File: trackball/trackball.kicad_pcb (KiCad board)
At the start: 2 copper layers, 15 x 13.4 mm, 13 parts, among them P8 CONN_7, U1 BU52012HFV-TR, U2 BU52012HFV-TR, U3 BU52012HFV-TR, U4 BU52012HFV-TR

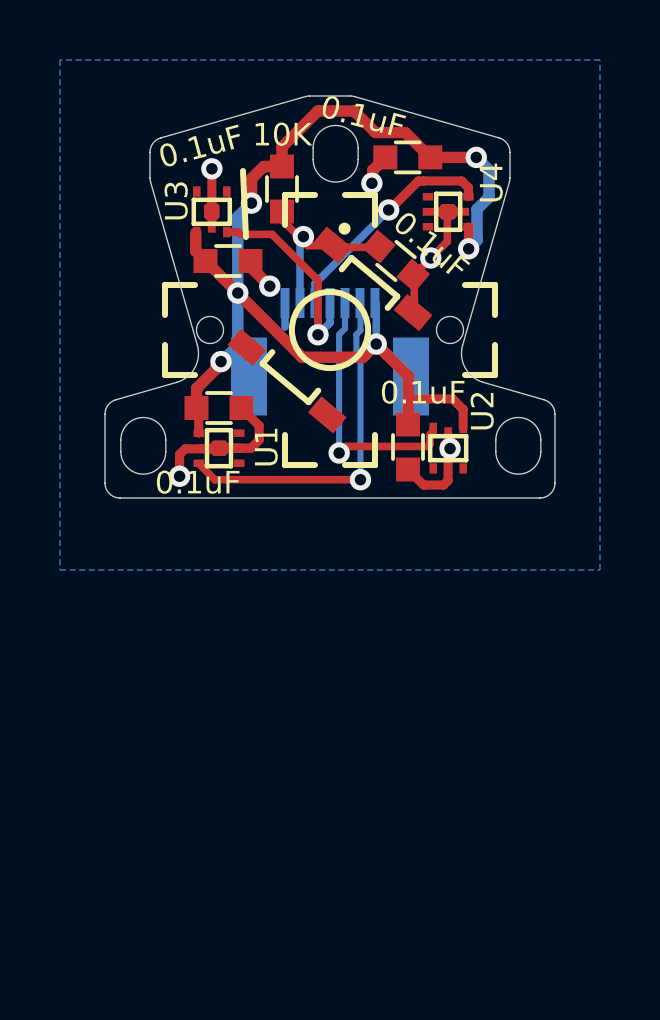
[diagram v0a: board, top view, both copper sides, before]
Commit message: Leave more space at the bottom of the board.
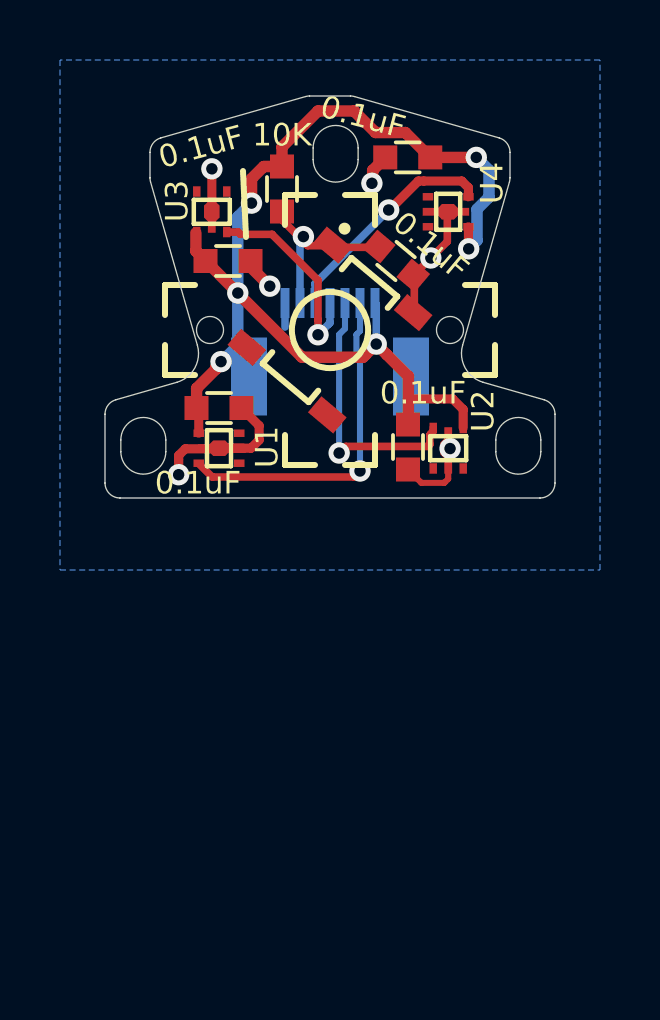
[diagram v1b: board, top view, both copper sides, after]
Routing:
- net GND: track 17.1 -> 16.5 mm
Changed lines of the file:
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@@
     (thickness 1.6)
     (drawings 42)
-    (tracks 140)
+    (tracks 141)
     (zones 0)
     (modules 13)
@@
     (pad_to_mask_clearance 0)
     (aux_axis_origin 0 0)
-    (visible_elements 7FFFEF7F)
+    (visible_elements 7FFFFF7F)
     (pcbplotparams
       (layerselection 0x00030_ffffffff)
@@
   (via (at 196.0626 144.627598) (size 0.7112) (drill 0.381) (layers F.Cu B.Cu) (net 1))
   (segment (start 196.0626 146.0754) (end 196.0626 144.627598) (width 0.3048) (layer F.Cu) (net 1))
-  (segment (start 203.1186 155.1686) (end 202.6 154.65) (width 0.3048) (layer F.Cu) (net 1))
-  (segment (start 203.7842 155.1686) (end 203.1186 155.1686) (width 0.3048) (layer F.Cu) (net 1))
-  (segment (start 203.9366 153.9494) (end 203.9366 155.0162) (width 0.3048) (layer F.Cu) (net 1))
-  (segment (start 203.9366 155.0162) (end 203.7842 155.1686) (width 0.3048) (layer F.Cu) (net 1))
   (via (at 197.993 148.5392) (size 0.7112) (drill 0.381) (layers F.Cu B.Cu) (net 1))
   (segment (start 197.35 147.8962) (end 197.993 148.5392) (width 0.381) (layer F.Cu) (net 1))
@@
   (segment (start 201.8404 144.26) (end 201.422 144.6784) (width 0.381) (layer F.Cu) (net 1))
   (via (at 204.002044 153.951866) (size 0.7112) (drill 0.381) (layers F.Cu B.Cu) (net 1))
-  (via (at 194.986061 154.876501) (size 0.7112) (drill 0.381) (layers F.Cu B.Cu) (net 1))
+  (segment (start 198.5 149.1) (end 198.5 149.9) (width 0.254) (layer B.Cu) (net 1))
+  (via (at 194.95467 154.823689) (size 0.7112) (drill 0.381) (layers F.Cu B.Cu) (net 1))
   (segment (start 196.3 153.94) (end 196.280601 153.959399) (width 0.3048) (layer F.Cu) (net 1))
   (segment (start 196.280601 153.959399) (end 195.178044 153.959399) (width 0.3048) (layer F.Cu) (net 1))
-  (segment (start 195.178044 153.959399) (end 194.986061 154.151382) (width 0.3048) (layer F.Cu) (net 1))
-  (segment (start 194.986061 154.373607) (end 194.986061 154.876501) (width 0.3048) (layer F.Cu) (net 1))
-  (segment (start 194.986061 154.151382) (end 194.986061 154.373607) (width 0.3048) (layer F.Cu) (net 1))
-  (segment (start 198.5 149.1) (end 198.5 149.9) (width 0.254) (layer B.Cu) (net 1))
+  (segment (start 195.178044 153.959399) (end 194.95467 154.182773) (width 0.3048) (layer F.Cu) (net 1))
+  (segment (start 194.95467 154.320795) (end 194.95467 154.823689) (width 0.3048) (layer F.Cu) (net 1))
+  (segment (start 194.95467 154.182773) (end 194.95467 154.320795) (width 0.3048) (layer F.Cu) (net 1))
+  (segment (start 203.808841 155.094801) (end 203.94 154.963642) (width 0.2032) (layer F.Cu) (net 1))
+  (segment (start 202.6 154.65) (end 203.044801 155.094801) (width 0.2032) (layer F.Cu) (net 1))
+  (segment (start 203.044801 155.094801) (end 203.808841 155.094801) (width 0.2032) (layer F.Cu) (net 1))
+  (segment (start 203.94 154.963642) (end 203.94 154.46) (width 0.2032) (layer F.Cu) (net 1))
   (segment (start 200.390425 147.2438) (end 200.335876 147.189251) (width 0.254) (layer F.Cu) (net 2))
   (segment (start 201.66967 147.16967) (end 201.59554 147.2438) (width 0.254) (layer F.Cu) (net 2))
@@
   (segment (start 199.11316 146.886077) (end 199 146.999237) (width 0.254) (layer B.Cu) (net 2))
   (segment (start 199 146.999237) (end 199 149.1) (width 0.254) (layer B.Cu) (net 2))
-  (via (at 201.0156 154.9908) (size 0.7112) (drill 0.381) (layers F.Cu B.Cu) (net 3))
-  (segment (start 196.1642 154.9908) (end 201.0156 154.9908) (width 0.254) (layer F.Cu) (net 3))
-  (segment (start 195.6308 154.4574) (end 196.1642 154.9908) (width 0.254) (layer F.Cu) (net 3))
-  (segment (start 201.0156 150.01774) (end 201.0156 149.2156) (width 0.2032) (layer B.Cu) (net 3))
-  (segment (start 200.880733 150.152607) (end 201.0156 150.01774) (width 0.2032) (layer B.Cu) (net 3))
-  (segment (start 200.880733 150.786593) (end 200.880733 150.152607) (width 0.2032) (layer B.Cu) (net 3))
-  (segment (start 201.0156 154.9908) (end 201.0156 150.92146) (width 0.2032) (layer B.Cu) (net 3))
-  (segment (start 201.0156 150.92146) (end 200.880733 150.786593) (width 0.2032) (layer B.Cu) (net 3))
-  (segment (start 201.0156 149.2156) (end 201 149.2) (width 0.2032) (layer B.Cu) (net 3))
+  (via (at 201 154.7) (size 0.7112) (drill 0.381) (layers F.Cu B.Cu) (net 3))
+  (segment (start 200.880733 150.152607) (end 200.880733 150.786593) (width 0.2032) (layer B.Cu) (net 3))
+  (segment (start 201 150.90586) (end 201 154.197106) (width 0.2032) (layer B.Cu) (net 3))
+  (segment (start 200.880733 150.786593) (end 201 150.90586) (width 0.2032) (layer B.Cu) (net 3))
+  (segment (start 201 149.2) (end 201 150.03334) (width 0.2032) (layer B.Cu) (net 3))
+  (segment (start 201 150.03334) (end 200.880733 150.152607) (width 0.2032) (layer B.Cu) (net 3))
+  (segment (start 201 154.197106) (end 201 154.7) (width 0.2032) (layer B.Cu) (net 3))
+  (segment (start 200.8 154.9) (end 201 154.7) (width 0.254) (layer F.Cu) (net 3))
+  (segment (start 195.6308 154.4574) (end 196.0734 154.9) (width 0.254) (layer F.Cu) (net 3))
+  (segment (start 196.0734 154.9) (end 200.8 154.9) (width 0.254) (layer F.Cu) (net 3))
   (segment (start 202.6158 153.162) (end 202.6158 152.2984) (width 0.381) (layer F.Cu) (net 4))
   (segment (start 202.6158 152.2984) (end 204.089 152.2984) (width 0.3048) (layer F.Cu) (net 4))

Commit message: Remove excess resistor and capacitor.
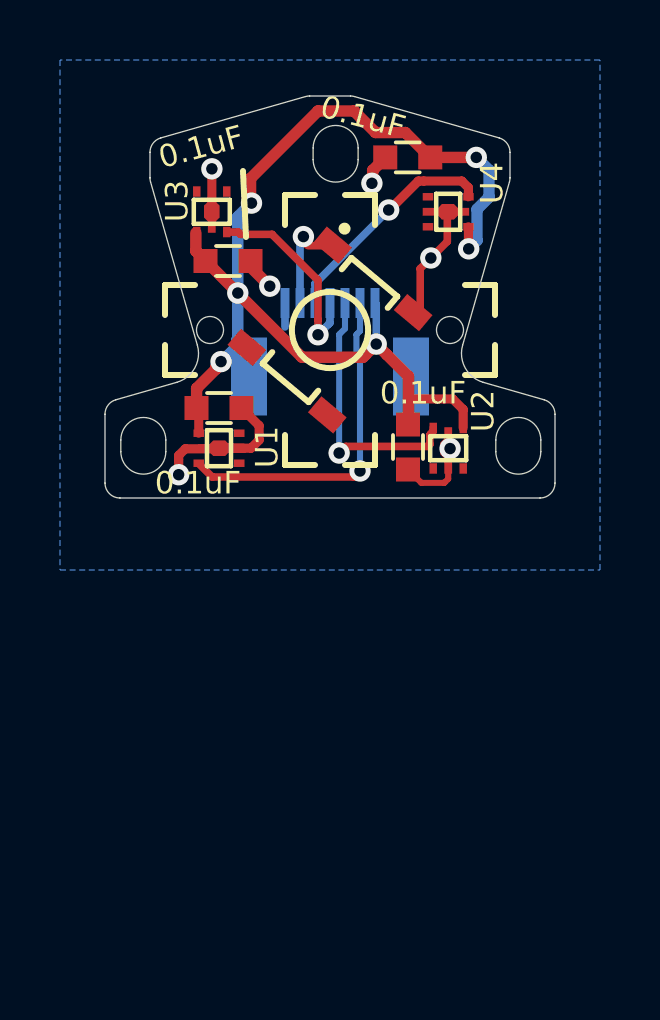
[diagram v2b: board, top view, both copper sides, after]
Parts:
- removed C5: 0.1uF, UGL:SM0603
- removed R5: 10K, UGL:SM0603
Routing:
- net /TB_BTN: track 6.82 -> 4.01 mm
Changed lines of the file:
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@@
     (thickness 1.6)
     (drawings 42)
-    (tracks 141)
+    (tracks 134)
     (zones 0)
-    (modules 13)
+    (modules 11)
     (nets 16)
   )
@@
   )
   (setup
-    (last_trace_width 0.2032)
+    (last_trace_width 0.254)
     (user_trace_width 0.2032)
     (user_trace_width 0.254)
@@
   )
   (module UGL:SM0603 (layer F.Cu)
-    (at 202.2 147.7 140)
-    (attr smd)
-    (fp_text reference C5 (at 0 0 140) (layer B.SilkS)
-      (effects (font (size 0.75 0.75) (thickness 0.15)) (justify mirror))
-    )
-    (fp_text value 0.1uF (at -0.565685 1.131371 140) (layer F.SilkS)
-      (effects (font (size 0.75 0.75) (thickness 0.15)))
-    )
-    (fp_line (start -0.4 -0.5) (end 0.4 -0.5) (layer F.SilkS) (width 0.127))
-    (fp_line (start 0.4 0.5) (end -0.4 0.5) (layer F.SilkS) (width 0.127))
-    (pad 1 smd rect (at -0.75 0 140) (size 0.8 0.8) (layers F.Cu F.Paste F.Mask)
-      (net 1 GND))
-    (pad 2 smd rect (at 0.75 0 140) (size 0.8 0.8) (layers F.Cu F.Paste F.Mask)
-      (net 2 /TB_BTN))
-    (model smd\resistors\R0603.wrl
-      (offset (xyz 0 0 0.02540000082496551))
-      (scale (xyz 0.5 0.5 0.5))
-      (rotate (xyz 0 0 0))
-    )
-  )
-  (module UGL:SM0603 (layer F.Cu)
-    (at 198.4 145.3 270)
-    (attr smd)
-    (fp_text reference R5 (at 0.1 0 270) (layer B.SilkS)
-      (effects (font (size 0.75 0.75) (thickness 0.15)) (justify mirror))
-    )
-    (fp_text value 10K (at -1.8 0) (layer F.SilkS)
-      (effects (font (size 0.75 0.75) (thickness 0.15)))
-    )
-    (fp_line (start -0.4 -0.5) (end 0.4 -0.5) (layer F.SilkS) (width 0.127))
-    (fp_line (start 0.4 0.5) (end -0.4 0.5) (layer F.SilkS) (width 0.127))
-    (pad 1 smd rect (at -0.75 0 270) (size 0.8 0.8) (layers F.Cu F.Paste F.Mask)
-      (net 4 +3V3))
-    (pad 2 smd rect (at 0.75 0 270) (size 0.8 0.8) (layers F.Cu F.Paste F.Mask)
-      (net 2 /TB_BTN))
-    (model smd\resistors\R0603.wrl
-      (offset (xyz 0 0 0.02540000082496551))
-      (scale (xyz 0.5 0.5 0.5))
-      (rotate (xyz 0 0 0))
-    )
-  )
-  (module UGL:SM0603 (layer F.Cu)
     (at 202.5904 144.2466)
     (attr smd)
@@
     (effects (font (size 0.75 0.75) (thickness 0.15)) (justify mirror))
   )
-  (segment (start 202.810749 148.310749) (end 202.73033 148.23033) (width 0.254) (layer F.Cu) (net 1))
-  (segment (start 202.810749 149.664124) (end 202.810749 148.310749) (width 0.254) (layer F.Cu) (net 1))
-  (segment (start 203.36126 147.5994) (end 202.73033 148.23033) (width 0.254) (layer F.Cu) (net 1))
-  (via (at 203.36126 147.5994) (size 0.7112) (drill 0.381) (layers F.Cu B.Cu) (net 1))
   (segment (start 197.11 153.94) (end 196.0974 153.94) (width 0.3048) (layer F.Cu) (net 1))
   (segment (start 196.0974 153.94) (end 196.088 153.9306) (width 0.3048) (layer F.Cu) (net 1))
@@
   (segment (start 203.044801 155.094801) (end 203.808841 155.094801) (width 0.2032) (layer F.Cu) (net 1))
   (segment (start 203.94 154.963642) (end 203.94 154.46) (width 0.2032) (layer F.Cu) (net 1))
+  (via (at 203.36126 147.5994) (size 0.7112) (drill 0.381) (layers F.Cu B.Cu) (net 1))
+  (segment (start 203.005661 147.954999) (end 203.005661 149.194339) (width 0.254) (layer F.Cu) (net 1))
+  (segment (start 203.36126 147.5994) (end 203.005661 147.954999) (width 0.254) (layer F.Cu) (net 1))
+  (segment (start 203.005661 149.194339) (end 202.8 149.4) (width 0.254) (layer F.Cu) (net 1))
   (segment (start 200.390425 147.2438) (end 200.335876 147.189251) (width 0.254) (layer F.Cu) (net 2))
-  (segment (start 201.66967 147.16967) (end 201.59554 147.2438) (width 0.254) (layer F.Cu) (net 2))
-  (segment (start 201.59554 147.2438) (end 200.390425 147.2438) (width 0.254) (layer F.Cu) (net 2))
   (segment (start 200.085625 146.939) (end 200.335876 147.189251) (width 0.254) (layer F.Cu) (net 2))
   (segment (start 199.9996 146.939) (end 200.085625 146.939) (width 0.254) (layer F.Cu) (net 2))
-  (segment (start 198.4 146.33) (end 198.4 146.05) (width 0.254) (layer F.Cu) (net 2))
   (segment (start 200.335876 147.189251) (end 199.259251 147.189251) (width 0.254) (layer F.Cu) (net 2))
-  (segment (start 199.259251 147.189251) (end 198.4 146.33) (width 0.254) (layer F.Cu) (net 2))
-  (via (at 199.11316 146.886077) (size 0.7112) (drill 0.381) (layers F.Cu B.Cu) (net 2))
   (segment (start 199 147.0242) (end 199.1106 146.9136) (width 0.254) (layer B.Cu) (net 2))
   (segment (start 199.11316 146.886077) (end 199 146.999237) (width 0.254) (layer B.Cu) (net 2))
   (segment (start 199 146.999237) (end 199 149.1) (width 0.254) (layer B.Cu) (net 2))
+  (via (at 199.11316 146.886077) (size 0.7112) (drill 0.381) (layers F.Cu B.Cu) (net 2))
   (via (at 201 154.7) (size 0.7112) (drill 0.381) (layers F.Cu B.Cu) (net 3))
   (segment (start 200.880733 150.152607) (end 200.880733 150.786593) (width 0.2032) (layer B.Cu) (net 3))
@@
   (segment (start 196.9262 146.2278) (end 197.3834 145.7706) (width 0.381) (layer B.Cu) (net 4))
   (segment (start 196.9262 148.9964) (end 196.9262 146.2278) (width 0.381) (layer B.Cu) (net 4))
-  (segment (start 197.3834 145.7706) (end 197.3834 144.9578) (width 0.381) (layer F.Cu) (net 4))
-  (segment (start 197.7912 144.55) (end 198.4 144.55) (width 0.381) (layer F.Cu) (net 4))
-  (segment (start 197.3834 144.9578) (end 197.7912 144.55) (width 0.381) (layer F.Cu) (net 4))
   (segment (start 204.8764 144.2466) (end 204.8764 144.2466) (width 0.381) (layer B.Cu) (net 4))
   (via (at 204.8764 144.2466) (size 0.7112) (drill 0.381) (layers F.Cu B.Cu) (net 4))
@@
   (segment (start 195.625 152.675) (end 195.55 152.6) (width 0.3048) (layer F.Cu) (net 4))
   (segment (start 195.625 153.44) (end 195.625 152.675) (width 0.3048) (layer F.Cu) (net 4))
-  (segment (start 198.4 143.9) (end 198.4 144.5) (width 0.381) (layer F.Cu) (net 4))
-  (segment (start 199.6 142.7) (end 198.4 143.9) (width 0.381) (layer F.Cu) (net 4))
   (segment (start 200.8 142.7) (end 199.6 142.7) (width 0.381) (layer F.Cu) (net 4))
   (segment (start 203.3404 144.2466) (end 202.511853 143.418053) (width 0.381) (layer F.Cu) (net 4))
@@
   (segment (start 196.9262 148.7678) (end 199.066527 150.908127) (width 0.381) (layer F.Cu) (net 4))
   (segment (start 201.102607 150.908127) (end 201.185535 150.825199) (width 0.381) (layer F.Cu) (net 4))
+  (segment (start 199.6 142.7) (end 197.35 144.95) (width 0.381) (layer F.Cu) (net 4))
+  (segment (start 197.35 144.95) (end 197.35 145.75) (width 0.381) (layer F.Cu) (net 4))
   (via (at 200.3044 154.1018) (size 0.7112) (drill 0.381) (layers F.Cu B.Cu) (net 5))
   (segment (start 203.44 153.3792) (end 203.44 153.265) (width 0.254) (layer F.Cu) (net 5))

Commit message: Bump trackball version number to 1.1.0
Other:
- board text added: "v1.1.0"
- board text removed: "v1.0.0"
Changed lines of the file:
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@@
   (title_block
     (title "UHK Key Cluster Module - Trackball Board")
-    (rev 1.0.0)
+    (rev 1.1.0)
     (company "Ultimate Gadget Laboratories Kft.")
   )
@@
   (gr_arc (start 205.382248 150.782505) (end 204.420921 150.506909) (angle -90) (layer Edge.Cuts) (width 0.01))
   (gr_arc (start 200.187782 143.931454) (end 200.937782 143.931454) (angle -180) (layer Edge.Cuts) (width 0.01))
-  (gr_text v1.0.0 (at 195.9 143.9 17) (layer B.SilkS)
+  (gr_text v1.1.0 (at 195.9 143.9 17) (layer B.SilkS)
     (effects (font (size 0.75 0.75) (thickness 0.15)) (justify mirror))
   )

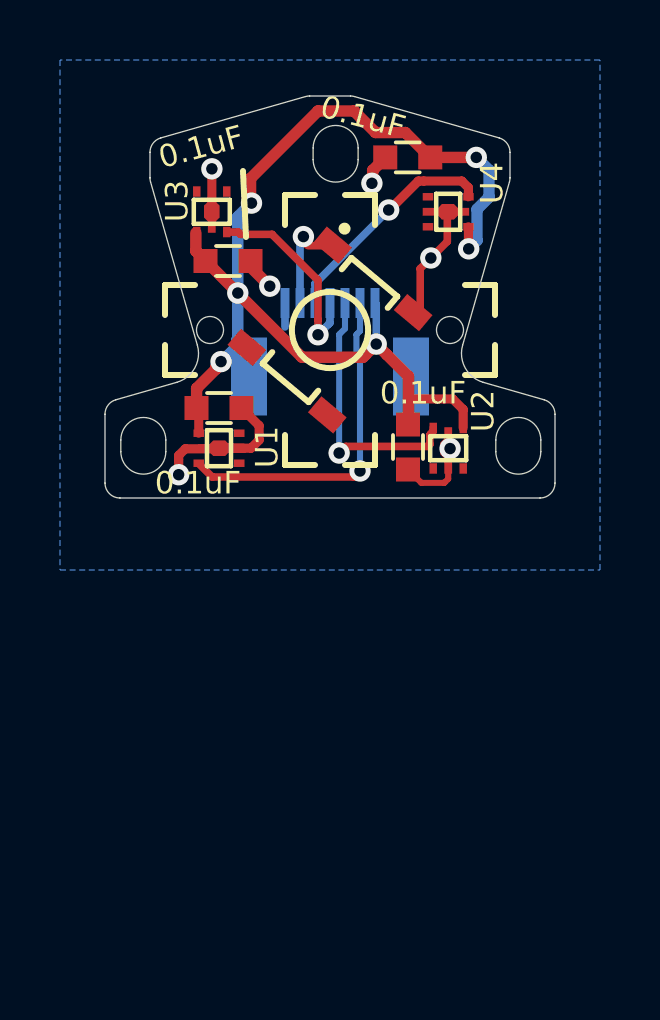
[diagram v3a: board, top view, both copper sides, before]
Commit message: Redesign panel with TLE4964.
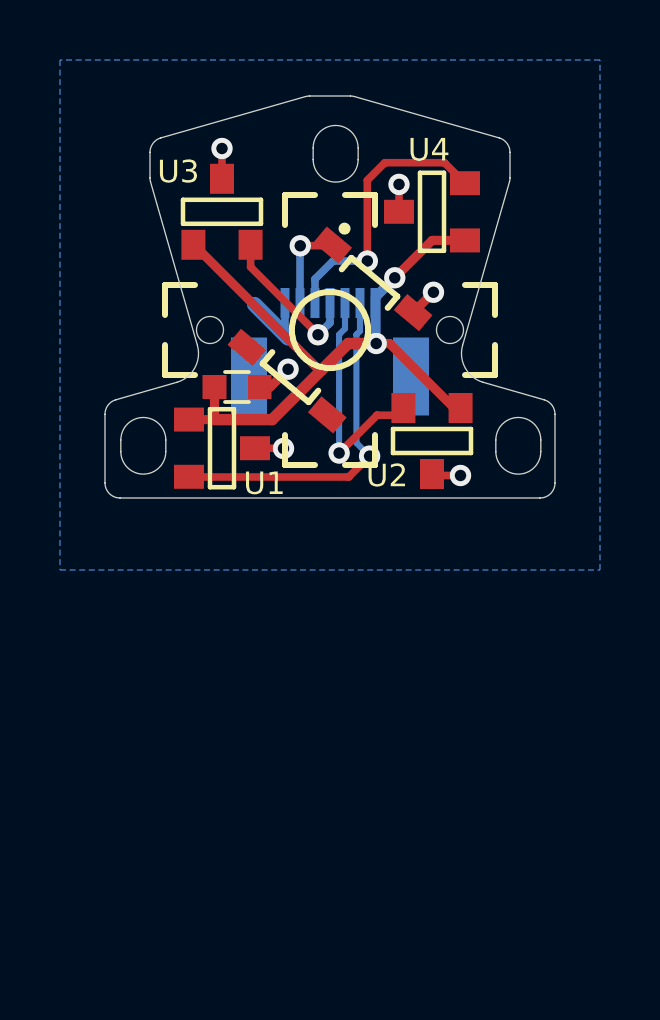
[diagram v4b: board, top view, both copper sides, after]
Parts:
- removed C2, C3, C4: 0.1uF, UGL:SM0603
- U1, U2, U3, U4: value BU52012HFV-TR -> TLE4964-5M; footprint UGL:HVSOF5 -> UGL:SOT-23
- moved C1 0.92 mm to (196.9, 151.9)
- moved U2 0.59 mm to (203.4, 153.7)
- moved U4 0.54 mm to (203.4, 146.1)
- moved U3 0.34 mm to (196.4, 146.1)
- moved U1 0.10 mm to (196.4, 153.9)
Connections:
- P8 pad : GND -> (no net)
- U1 pad 1: Net-(U1-Pad1) -> +3V3
- U1 pad 2: GND -> /TB_LEFT
- U1 pad 3: Net-(U1-Pad3) -> GND
- U2 pad 1: Net-(U2-Pad1) -> +3V3
- U2 pad 2: GND -> /TB_DOWN
- U2 pad 3: Net-(U2-Pad3) -> GND
- U3 pad 1: Net-(U3-Pad1) -> +3V3
- U3 pad 2: GND -> /TB_UP
- U3 pad 3: Net-(U3-Pad3) -> GND
- U4 pad 1: Net-(U4-Pad1) -> +3V3
- U4 pad 2: GND -> /TB_RIGHT
- U4 pad 3: Net-(U4-Pad3) -> GND
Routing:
- net +3V3: track 38.3 -> 23.6 mm, vias 6 -> 2
- net GND: track 16.2 -> 8.44 mm
- net /TB_RIGHT: track 7.51 -> 9.58 mm
- net /TB_UP: track 6.75 -> 5.15 mm
- net /TB_DOWN: track 8.92 -> 7.85 mm
